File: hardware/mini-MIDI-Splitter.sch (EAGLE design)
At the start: 45 parts, among them IC1 REG1117, IC2 4050D, IC3 PIC12F1822SO08, IC4 6N138, X1 DIN5PIN, X2 DIN5PIN, X3 DIN5PIN, X4 DIN5PIN, X5 DIN5PIN, X6 DIN5PIN, X7 VERTICAL_3_5MM_SOCKET

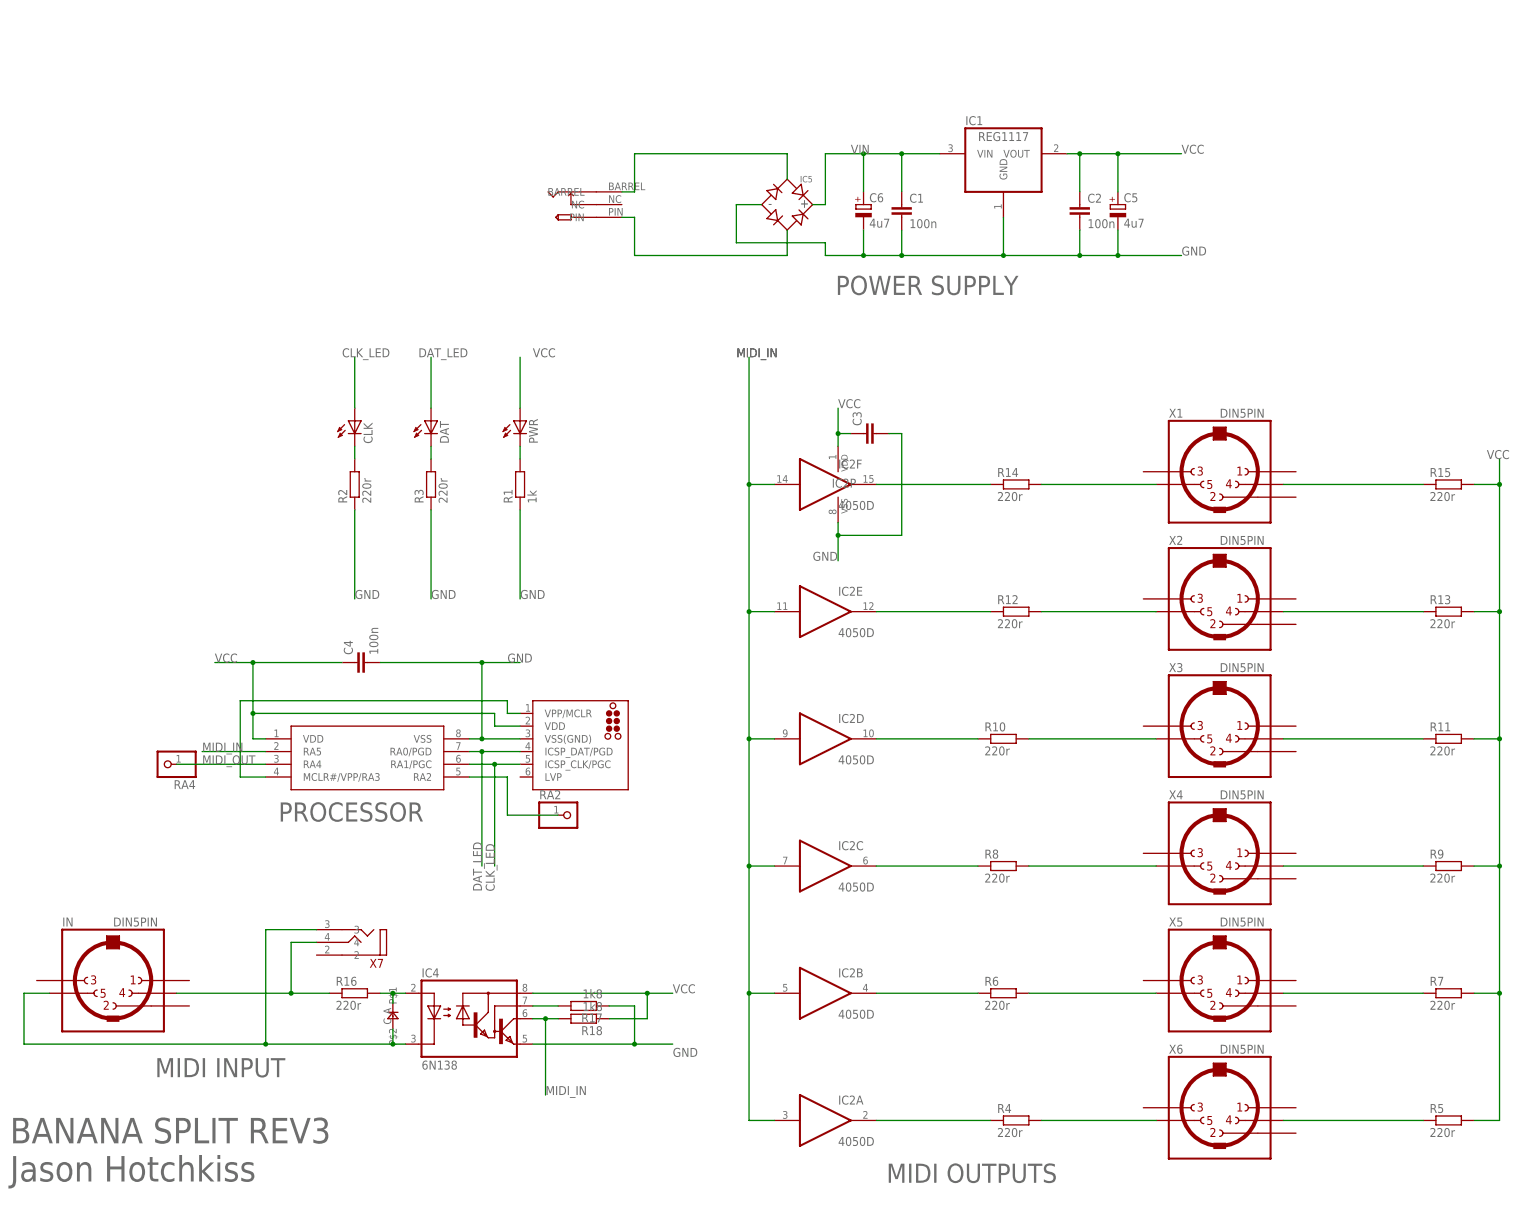
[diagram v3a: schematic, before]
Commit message: V4 - Grounding output GND pins!
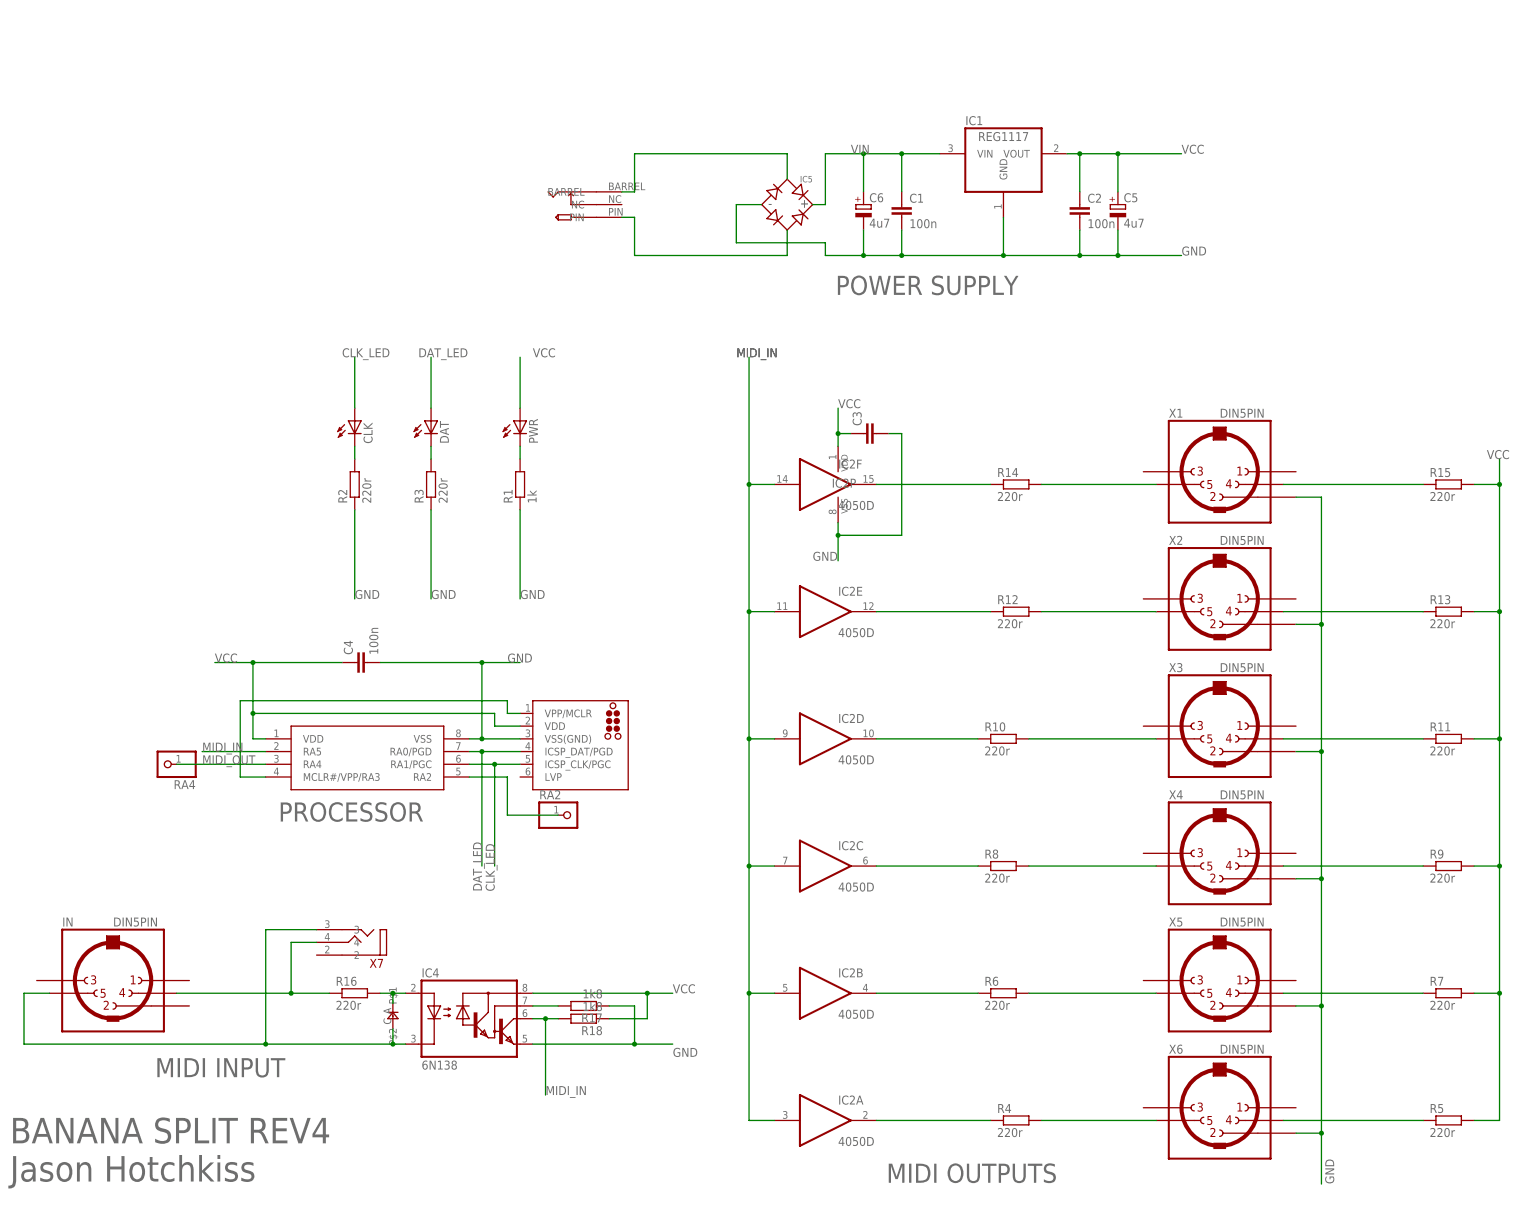
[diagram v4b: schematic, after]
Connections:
- net GND: now also X1.2, X2.2, X3.2, X4.2, X5.2, X6.2
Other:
- note added: "BANANA SPLIT REV4"
- note removed: "BANANA SPLIT REV3"
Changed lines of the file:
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@@
 <text x="-39.878" y="-75.184" size="3.81" layer="95">MIDI INPUT</text>
 <text x="-15.24" y="-24.13" size="3.81" layer="95">PROCESSOR</text>
-<text x="-68.834" y="-88.392" size="5.08" layer="95">BANANA SPLIT REV3</text>
+<text x="-68.834" y="-88.392" size="5.08" layer="95">BANANA SPLIT REV4</text>
 <text x="-68.834" y="-96.012" size="5.08" layer="95">Jason Hotchkiss</text>
 </plain>
@@
 <label x="30.48" y="7.62" size="1.778" layer="95"/>
 </segment>
-</net>
+<segment>
+<pinref part="X1" gate="G$1" pin="2"/>
+<wire x1="187.96" y1="40.64" x2="193.04" y2="40.64" width="0.1524" layer="91"/>
+<wire x1="193.04" y1="40.64" x2="193.04" y2="15.24" width="0.1524" layer="91"/>
+<pinref part="X2" gate="G$1" pin="2"/>
+<wire x1="193.04" y1="15.24" x2="193.04" y2="-10.16" width="0.1524" layer="91"/>
+<wire x1="193.04" y1="-10.16" x2="193.04" y2="-35.56" width="0.1524" layer="91"/>
+<wire x1="193.04" y1="-35.56" x2="193.04" y2="-60.96" width="0.1524" layer="91"/>
+<wire x1="193.04" y1="-60.96" x2="193.04" y2="-86.36" width="0.1524" layer="91"/>
+<wire x1="193.04" y1="-86.36" x2="193.04" y2="-96.52" width="0.1524" layer="91"/>
+<wire x1="187.96" y1="15.24" x2="193.04" y2="15.24" width="0.1524" layer="91"/>
+<junction x="193.04" y="15.24"/>
+<pinref part="X3" gate="G$1" pin="2"/>
+<wire x1="187.96" y1="-10.16" x2="193.04" y2="-10.16" width="0.1524" layer="91"/>
+<junction x="193.04" y="-10.16"/>
+<pinref part="X4" gate="G$1" pin="2"/>
+<wire x1="187.96" y1="-35.56" x2="193.04" y2="-35.56" width="0.1524" layer="91"/>
+<junction x="193.04" y="-35.56"/>
+<pinref part="X5" gate="G$1" pin="2"/>
+<wire x1="187.96" y1="-60.96" x2="193.04" y2="-60.96" width="0.1524" layer="91"/>
+<junction x="193.04" y="-60.96"/>
+<pinref part="X6" gate="G$1" pin="2"/>
+<wire x1="187.96" y1="-86.36" x2="193.04" y2="-86.36" width="0.1524" layer="91"/>
+<junction x="193.04" y="-86.36"/>
+<label x="195.58" y="-96.52" size="1.778" layer="95" rot="R90"/>
+</segment>
+</net>
